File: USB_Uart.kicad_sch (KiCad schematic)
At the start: 14 parts, among them J1 USB_B, U1 CP2104

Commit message: Add files via upload
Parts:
- removed C2: .1uf, symbol Device:C_Small
- removed D?: LED_Red_Blue, symbol Device:LED_Dual_KAKA
- added D1: Blue, symbol Device:LED_Small
- added D2: Red, symbol Device:LED_Small
- added U2: TPD4EUSB30, Package_SON:USON-10_2.5x1.0mm_P0.5mm, symbol Power_Protection:TPD4EUSB30
- R3: renamed from R?; value 330 -> 3k
- R4: renamed from R?; value 150 -> 1.5k
- gave numbers to parts that had none: 5
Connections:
- net D+: now also U2.1 (D1+)
- net D-: now also U2.2 (D1-)
- net GND: now also U2.3 (GND), U2.8 (GND)
- net Rx: now also D2.2 (A), U2.5 (D2-)
- net Tx: now also D1.2 (A), U2.4 (D2+)
- net at R3.1: now also D1.1 (K)
- net at R4.1: now also D2.1 (K)
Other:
- moved on the sheet: C1

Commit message: Update Schematic, start footprint layout
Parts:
- C1, C3: footprint (none) -> Capacitor_SMD:C_0402_1005Metric
- D1, D2, D3: footprint (none) -> LED_SMD:LED_0603_1608Metric
- J1: footprint (none) -> Connector_USB:USB_B_Lumberg_2411_02_Horizontal
- J2: footprint (none) -> Connector_PinHeader_2.54mm:PinHeader_1x10_P2.54mm_Vertical
- J3, J4: footprint (none) -> Connector_PinHeader_2.54mm:PinHeader_1x04_P2.54mm_Vertical
- R1, R2, R3, R4: footprint (none) -> Resistor_SMD:R_0402_1005Metric
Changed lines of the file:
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@@
       (effects (font (size 1.27 1.27)) (justify left))
     )
-    (property "Footprint" "" (id 2) (at 109.22 43.18 0)
+    (property "Footprint" "Connector_PinHeader_2.54mm:PinHeader_1x10_P2.54mm_Vertical" (id 2) (at 109.22 43.18 0)
       (effects (font (size 1.27 1.27)) hide)
     )
@@
     (property "Reference" "R3" (id 0) (at 45.72 67.31 90))
     (property "Value" "3k" (id 1) (at 45.72 68.58 90))
-    (property "Footprint" "" (id 2) (at 45.72 68.58 0)
+    (property "Footprint" "Resistor_SMD:R_0402_1005Metric" (id 2) (at 45.72 68.58 0)
       (effects (font (size 1.27 1.27)) hide)
     )
@@
     (property "Reference" "D1" (id 0) (at 40.64 66.04 0))
     (property "Value" "Blue" (id 1) (at 44.45 69.85 0))
-    (property "Footprint" "" (id 2) (at 40.64 68.58 90)
+    (property "Footprint" "LED_SMD:LED_0603_1608Metric" (id 2) (at 40.64 68.58 90)
       (effects (font (size 1.27 1.27)) hide)
     )
@@
       (effects (font (size 1.27 1.27)) (justify left))
     )
-    (property "Footprint" "" (id 2) (at 45.72 30.48 0)
+    (property "Footprint" "Resistor_SMD:R_0402_1005Metric" (id 2) (at 45.72 30.48 0)
       (effects (font (size 1.27 1.27)) hide)
     )
@@
     (property "Reference" "J1" (id 0) (at 36.83 39.37 0))
     (property "Value" "USB_B" (id 1) (at 36.83 41.91 0))
-    (property "Footprint" "" (id 2) (at 40.64 52.07 0)
+    (property "Footprint" "Connector_USB:USB_B_Lumberg_2411_02_Horizontal" (id 2) (at 40.64 52.07 0)
       (effects (font (size 1.27 1.27)) hide)
     )
@@
     (property "Reference" "R4" (id 0) (at 45.72 72.39 90))
     (property "Value" "1.5k" (id 1) (at 45.72 73.66 90))
-    (property "Footprint" "" (id 2) (at 45.72 73.66 0)
+    (property "Footprint" "Resistor_SMD:R_0402_1005Metric" (id 2) (at 45.72 73.66 0)
       (effects (font (size 1.27 1.27)) hide)
     )
@@
       (effects (font (size 1.27 1.27)) (justify left))
     )
-    (property "Footprint" "" (id 2) (at 59.69 30.48 0)
+    (property "Footprint" "Resistor_SMD:R_0402_1005Metric" (id 2) (at 59.69 30.48 0)
       (effects (font (size 1.27 1.27)) hide)
     )
@@
       (effects (font (size 1.27 1.27)) (justify left))
     )
-    (property "Footprint" "" (id 2) (at 53.34 30.48 0)
+    (property "Footprint" "Capacitor_SMD:C_0402_1005Metric" (id 2) (at 53.34 30.48 0)
       (effects (font (size 1.27 1.27)) hide)
     )
@@
     (property "Reference" "D2" (id 0) (at 40.64 71.12 0))
     (property "Value" "Red" (id 1) (at 44.45 76.2 0))
-    (property "Footprint" "" (id 2) (at 40.64 73.66 90)
+    (property "Footprint" "LED_SMD:LED_0603_1608Metric" (id 2) (at 40.64 73.66 90)
       (effects (font (size 1.27 1.27)) hide)
     )
@@
       (effects (font (size 1.27 1.27)) (justify right))
     )
-    (property "Footprint" "" (id 2) (at 45.72 36.83 0)
+    (property "Footprint" "LED_SMD:LED_0603_1608Metric" (id 2) (at 45.72 36.83 0)
       (effects (font (size 1.27 1.27)) hide)
     )
@@
       (effects (font (size 1.27 1.27)) (justify left))
     )
-    (property "Footprint" "" (id 2) (at 59.69 78.74 0)
+    (property "Footprint" "Capacitor_SMD:C_0402_1005Metric" (id 2) (at 59.69 78.74 0)
       (effects (font (size 1.27 1.27)) hide)
     )
@@
       (effects (font (size 1.27 1.27)) (justify left))
     )
-    (property "Footprint" "" (id 2) (at 109.22 63.5 0)
+    (property "Footprint" "Connector_PinHeader_2.54mm:PinHeader_1x04_P2.54mm_Vertical" (id 2) (at 109.22 63.5 0)
       (effects (font (size 1.27 1.27)) hide)
     )
@@
       (effects (font (size 1.27 1.27)) (justify left))
     )
-    (property "Footprint" "" (id 2) (at 109.22 77.47 0)
+    (property "Footprint" "Connector_PinHeader_2.54mm:PinHeader_1x04_P2.54mm_Vertical" (id 2) (at 109.22 77.47 0)
       (effects (font (size 1.27 1.27)) hide)
     )
@@
     )
     (path "/7f26665a-402a-4dfa-86e6-1904a0a621c3"
-      (reference "C1") (unit 1) (value "1uf") (footprint "")
+      (reference "C1") (unit 1) (value "1uf") (footprint "Capacitor_SMD:C_0402_1005Metric")
     )
     (path "/dd192b81-22be-462a-b311-808b99931d1f"
-      (reference "C3") (unit 1) (value "4.7uf") (footprint "")
+      (reference "C3") (unit 1) (value "4.7uf") (footprint "Capacitor_SMD:C_0402_1005Metric")
     )
     (path "/4e9b2216-3ad9-48cf-a9d1-e8ab2fe7aee9"
-      (reference "D1") (unit 1) (value "Blue") (footprint "")
+      (reference "D1") (unit 1) (value "Blue") (footprint "LED_SMD:LED_0603_1608Metric")
     )
     (path "/8510da6a-7c57-4923-8c16-80f312d81352"
-      (reference "D2") (unit 1) (value "Red") (footprint "")
+      (reference "D2") (unit 1) (value "Red") (footprint "LED_SMD:LED_0603_1608Metric")
     )
     (path "/9744c75a-0682-4ad0-a358-a179b3201c01"
-      (reference "D3") (unit 1) (value "LED") (footprint "")
+      (reference "D3") (unit 1) (value "LED") (footprint "LED_SMD:LED_0603_1608Metric")
     )
     (path "/5782c7a9-dc2a-4da3-9f98-091d9b19b9bb"
-      (reference "J1") (unit 1) (value "USB_B") (footprint "")
+      (reference "J1") (unit 1) (value "USB_B") (footprint "Connector_USB:USB_B_Lumberg_2411_02_Horizontal")
     )
     (path "/0216027c-e4e3-4ccc-9069-43fb81a376cd"
-      (reference "J2") (unit 1) (value "Conn_01x10") (footprint "")
+      (reference "J2") (unit 1) (value "Conn_01x10") (footprint "Connector_PinHeader_2.54mm:PinHeader_1x10_P2.54mm_Vertical")
     )
     (path "/de77d655-907e-49be-b9a4-cbf715d29dca"
-      (reference "J3") (unit 1) (value "Conn_01x04") (footprint "")
+      (reference "J3") (unit 1) (value "Conn_01x04") (footprint "Connector_PinHeader_2.54mm:PinHeader_1x04_P2.54mm_Vertical")
     )
     (path "/e8566fd5-eae9-422b-9ec5-6ed3ad44437f"
-      (reference "J4") (unit 1) (value "Conn_01x04") (footprint "")
+      (reference "J4") (unit 1) (value "Conn_01x04") (footprint "Connector_PinHeader_2.54mm:PinHeader_1x04_P2.54mm_Vertical")
     )
     (path "/5cb680a9-21cd-4af4-99c0-62f322dcedab"
-      (reference "R1") (unit 1) (value "4.7k") (footprint "")
+      (reference "R1") (unit 1) (value "4.7k") (footprint "Resistor_SMD:R_0402_1005Metric")
     )
     (path "/4ff2d74e-9315-45bd-b0eb-d7841c8d67c4"
-      (reference "R2") (unit 1) (value "1k") (footprint "")
+      (reference "R2") (unit 1) (value "1k") (footprint "Resistor_SMD:R_0402_1005Metric")
     )
     (path "/2fa66272-c2af-4d90-8c74-8c881d6c6237"
-      (reference "R3") (unit 1) (value "3k") (footprint "")
+      (reference "R3") (unit 1) (value "3k") (footprint "Resistor_SMD:R_0402_1005Metric")
     )
     (path "/5b06160b-9828-41c6-a202-1fde0cbf366b"
-      (reference "R4") (unit 1) (value "1.5k") (footprint "")
+      (reference "R4") (unit 1) (value "1.5k") (footprint "Resistor_SMD:R_0402_1005Metric")
     )
     (path "/e77f1a97-5599-4bf9-9a83-6ffeaef8420a"

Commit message: Layout footprints,  Adjust schematic
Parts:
- U2: footprint Package_SON:USON-10_2.5x1.0mm_P0.5mm -> Package_TO_SOT_SMD:SOT-363_SC-70-6
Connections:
- net D+: now also U2.3 (D1-); no longer U2.1 (D1+)
- net D-: now also U2.1 (D1+); no longer U2.2 (D1-)
- net GND: now also U2.2 (GND); no longer U2.3 (GND), U2.8 (GND)
- net Rx: now also U2.6 (NC); no longer U2.5 (D2-)

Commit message: Switch to USB-B-Micro, add routing
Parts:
- removed J1: USB_B, Connector_USB:USB_B_Lumberg_2411_02_Horizontal, symbol Connector:USB_B
- added C?: 4.7uf, Capacitor_SMD:C_0402_1005Metric, symbol Device:C_Small
- added J5: USB_B_Mini, Connector_USB:USB_Micro-B_Molex-105017-0001, symbol Connector:USB_B_Mini
- J3: footprint Connector_PinHeader_2.54mm:PinHeader_1x04_P2.54mm_Vertical -> Connector_Molex:Molex_KK-254_AE-6410-04A_1x04_P2.54mm_Vertical
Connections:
- net D+: now also J5.3 (D+)
- net D-: now also J5.2 (D-)
- net GND: now also R2.2, C?.2, J5.5 (GND), J5.6 (Shield); no longer D3.1 (K)
- net Rx: now also D1.2 (A), J3.2 (Pin_2); no longer D2.2 (A), J3.3 (Pin_3)
- net Tx: now also D2.2 (A), J3.3 (Pin_3); no longer D1.2 (A), J3.2 (Pin_2)
- net VBUS: now also C?.1, J5.1 (VBUS)
- net Vdd: now also D3.2 (A); no longer R2.1
- net Vcc renamed VDD
- new net: D3.1 (K), R2.1
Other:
- moved on the sheet: D3, R2

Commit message: Add files via upload
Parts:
- gave numbers to parts that had none: 1
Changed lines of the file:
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@@
   (symbol (lib_id "power:GND") (at 36.83 27.94 0) (unit 1)
     (in_bom yes) (on_board yes)
-    (property "Reference" "#PWR?" (id 0) (at 36.83 34.29 0)
+    (property "Reference" "#PWR0102" (id 0) (at 36.83 34.29 0)
       (effects (font (size 1.27 1.27)) hide)
     )
@@
   (symbol (lib_id "Device:C_Small") (at 36.83 25.4 0) (unit 1)
     (in_bom yes) (on_board yes)
-    (property "Reference" "C?" (id 0) (at 39.37 25.4 0)
+    (property "Reference" "C2" (id 0) (at 39.37 25.4 0)
       (effects (font (size 1.27 1.27)) (justify left))
     )
@@
       (reference "#PWR0101") (unit 1) (value "GND") (footprint "")
     )
+    (path "/3f38e86c-bb7e-4e76-a503-06d1e902ac1b"
+      (reference "#PWR0102") (unit 1) (value "GND") (footprint "")
+    )
     (path "/ee7a20e8-ec92-4b87-abf0-ac524355a94d"
       (reference "#PWR0103") (unit 1) (value "GND") (footprint "")
@@
       (reference "#PWR0108") (unit 1) (value "GND") (footprint "")
     )
-    (path "/3f38e86c-bb7e-4e76-a503-06d1e902ac1b"
-      (reference "#PWR?") (unit 1) (value "GND") (footprint "")
-    )
     (path "/7f26665a-402a-4dfa-86e6-1904a0a621c3"
       (reference "C1") (unit 1) (value "1uf") (footprint "Capacitor_SMD:C_0402_1005Metric")
     )
+    (path "/7ce2bf31-9258-4de9-bb68-9dc6bb16b718"
+      (reference "C2") (unit 1) (value "4.7uf") (footprint "Capacitor_SMD:C_0402_1005Metric")
+    )
     (path "/dd192b81-22be-462a-b311-808b99931d1f"
       (reference "C3") (unit 1) (value "4.7uf") (footprint "Capacitor_SMD:C_0402_1005Metric")
     )
-    (path "/7ce2bf31-9258-4de9-bb68-9dc6bb16b718"
-      (reference "C?") (unit 1) (value "4.7uf") (footprint "Capacitor_SMD:C_0402_1005Metric")
-    )
     (path "/4e9b2216-3ad9-48cf-a9d1-e8ab2fe7aee9"

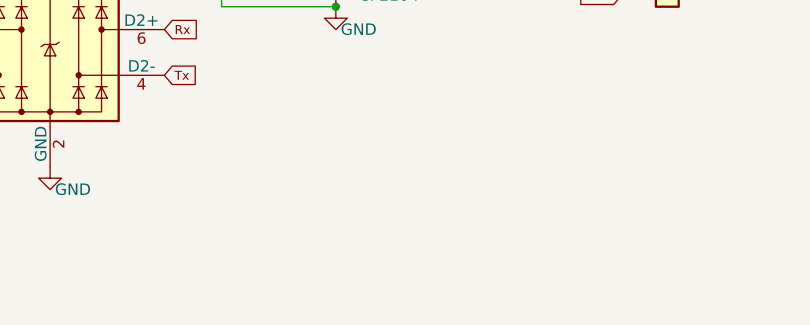
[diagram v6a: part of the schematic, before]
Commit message: Fine tuning traces and fills.  Added Silkscreen
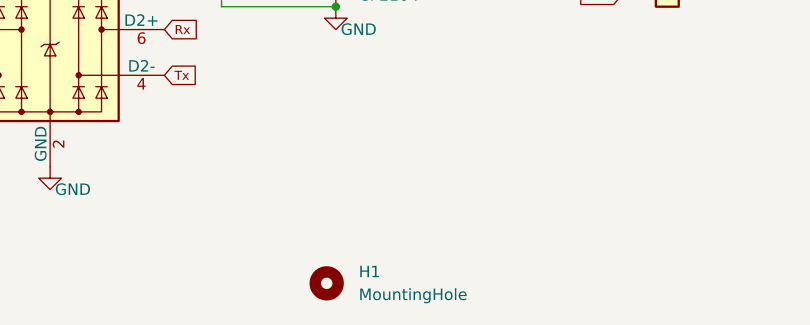
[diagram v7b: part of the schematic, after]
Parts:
- added H1: MountingHole, symbol Mechanical:MountingHole
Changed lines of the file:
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@@
     (pin "2")
+  )
+  (symbol (lib_id "Mechanical:MountingHole") (at 71.374 114.554 0) (unit 1)
+    (in_bom yes) (on_board yes) (fields_autoplaced)
+    (property "Reference" "H1" (id 0) (at 74.93 113.2839 0)
+      (effects (font (size 1.27 1.27)) (justify left))
+    )
+    (property "Value" "MountingHole" (id 1) (at 74.93 115.8239 0)
+      (effects (font (size 1.27 1.27)) (justify left))
+    )
+    (property "Footprint" "" (id 2) (at 71.374 114.554 0)
+      (effects (font (size 1.27 1.27)) hide)
+    )
+    (property "Datasheet" "~" (id 3) (at 71.374 114.554 0)
+      (effects (font (size 1.27 1.27)) hide)
+    )
   )
   (symbol (lib_id "power:GND") (at 104.14 68.58 0) (unit 1)
@@
       (reference "D3") (unit 1) (value "LED") (footprint "LED_SMD:LED_0603_1608Metric")
     )
+    (path "/5389a11a-7b98-4ae6-8b06-663ad19cd0e8"
+      (reference "H1") (unit 1) (value "MountingHole") (footprint "")
+    )
     (path "/0216027c-e4e3-4ccc-9069-43fb81a376cd"
